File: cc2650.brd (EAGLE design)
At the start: 50.8 x 22.9 mm, 19 parts, among them IC1 TPS73133DBVR, IC4 CC2650MODAMOHR, SW1 SPST_TACT-KMR2, SW3 SPST_TACT-KMR2

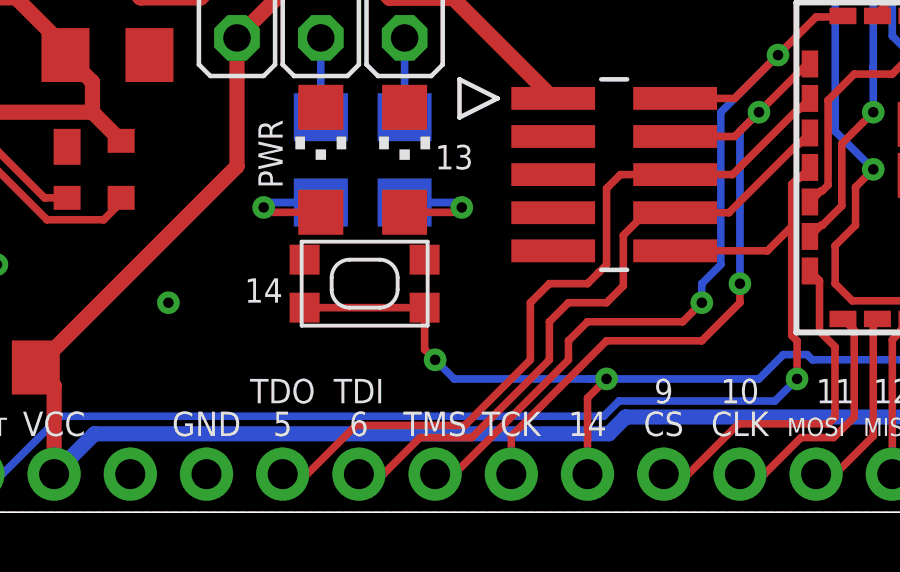
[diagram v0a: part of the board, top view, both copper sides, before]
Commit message: moved gpio button down from LEDs. reduced 'Team Rocket' font size on back so it doesn't interfere with resistors on back.
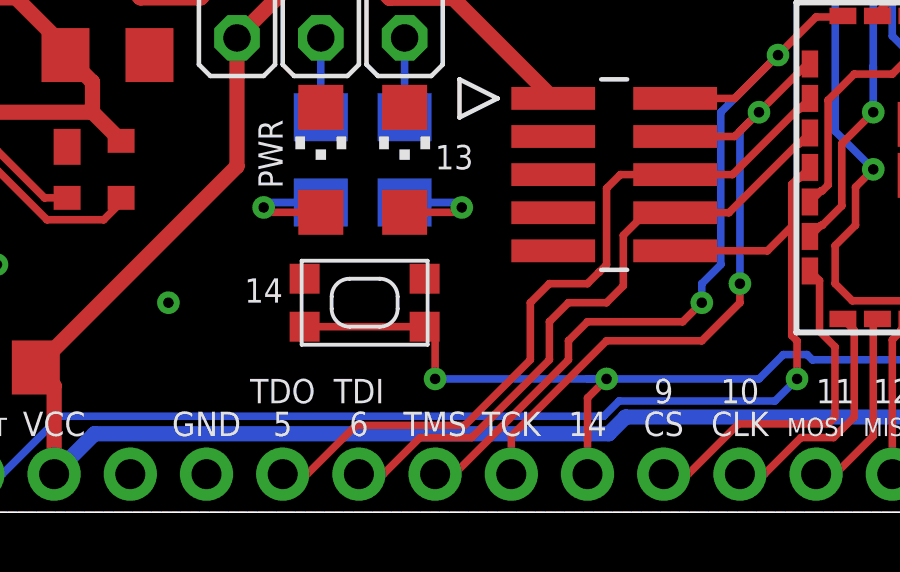
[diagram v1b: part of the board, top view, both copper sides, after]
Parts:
- moved SW3 0.63 mm to (19.2, 6.99)

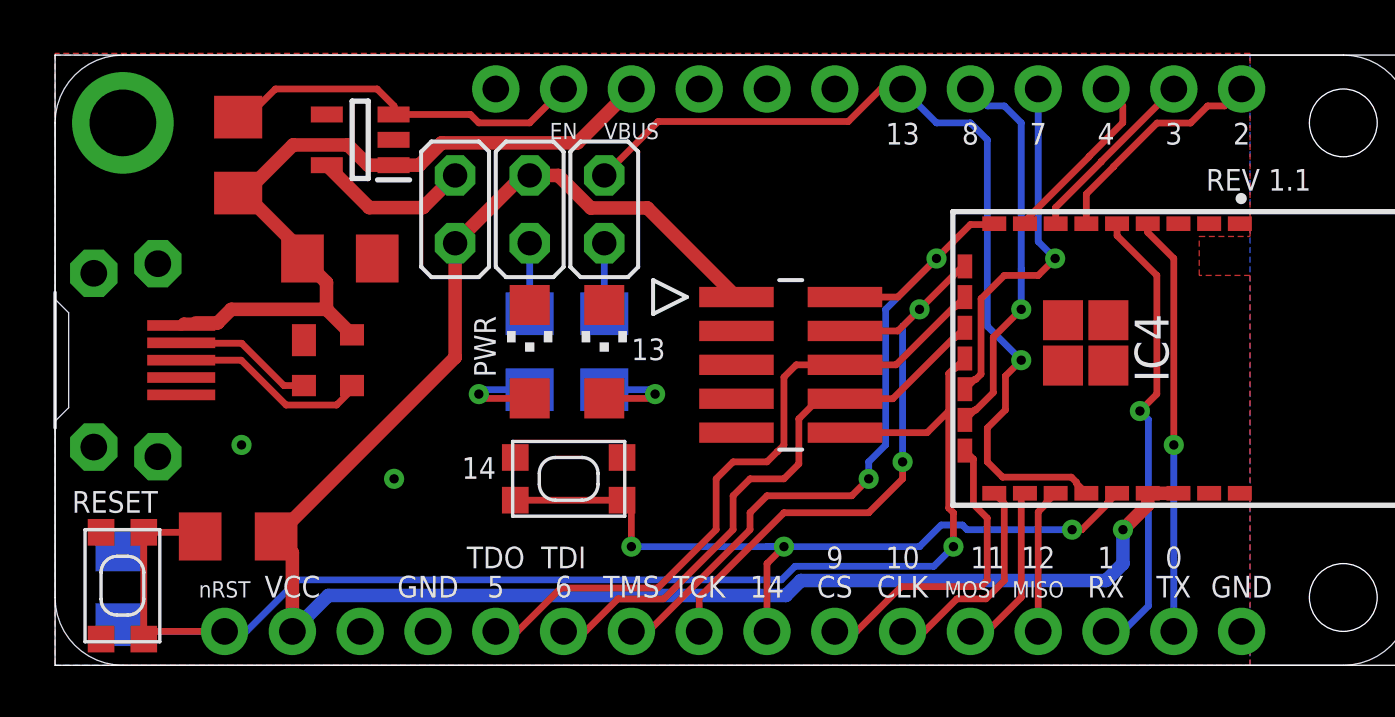
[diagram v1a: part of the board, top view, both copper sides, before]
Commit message: added extra gnd plane vias
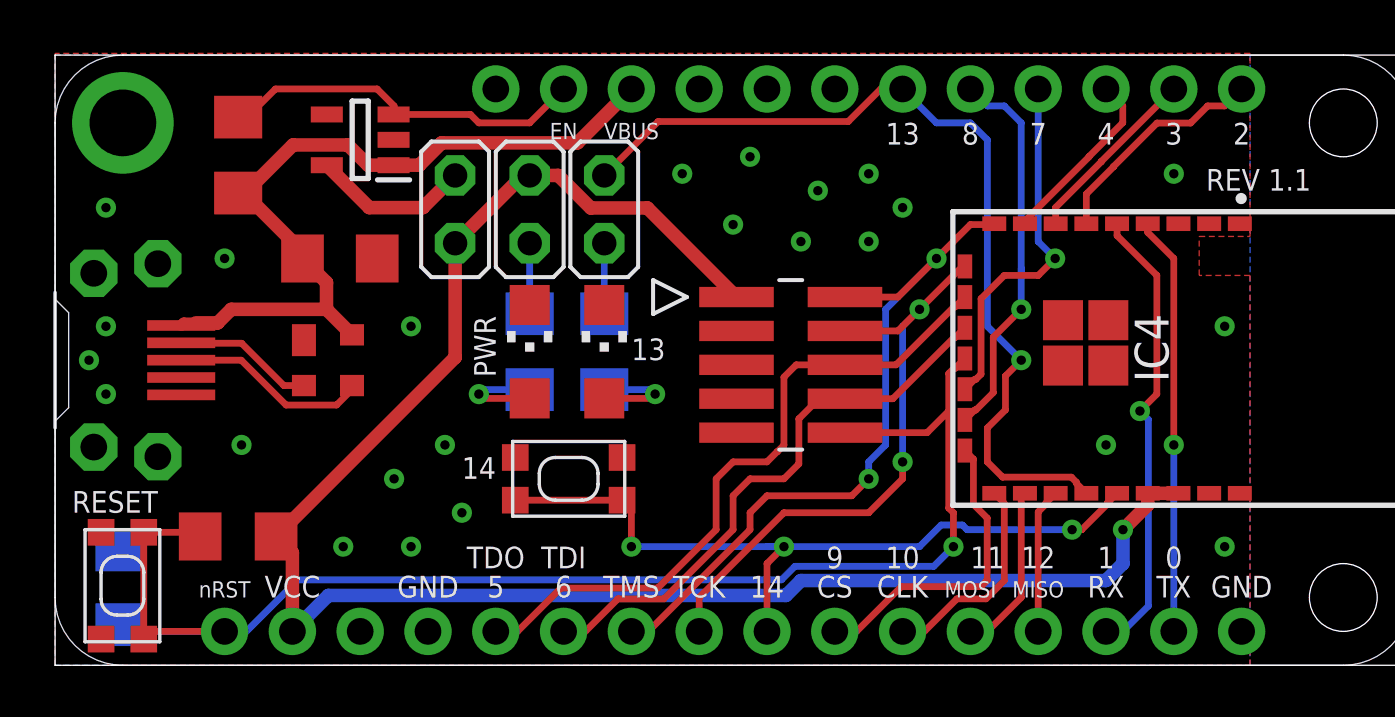
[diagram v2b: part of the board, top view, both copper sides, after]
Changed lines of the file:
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@@
 <via x="6.985" y="8.255" extent="1-16" drill="0.35"/>
 <via x="12.7" y="6.985" extent="1-16" drill="0.35"/>
+<via x="1.905" y="17.145" extent="1-16" drill="0.35"/>
+<via x="6.35" y="15.24" extent="1-16" drill="0.35"/>
+<via x="1.905" y="12.7" extent="1-16" drill="0.35"/>
+<via x="1.27" y="11.43" extent="1-16" drill="0.35"/>
+<via x="1.905" y="10.16" extent="1-16" drill="0.35"/>
+<via x="10.795" y="4.445" extent="1-16" drill="0.35"/>
+<via x="13.335" y="4.445" extent="1-16" drill="0.35"/>
+<via x="15.24" y="5.715" extent="1-16" drill="0.35"/>
+<via x="14.605" y="8.255" extent="1-16" drill="0.35"/>
+<via x="13.335" y="12.7" extent="1-16" drill="0.35"/>
+<via x="23.495" y="18.415" extent="1-16" drill="0.35"/>
+<via x="26.035" y="19.05" extent="1-16" drill="0.35"/>
+<via x="25.4" y="16.51" extent="1-16" drill="0.35"/>
+<via x="27.94" y="15.875" extent="1-16" drill="0.35"/>
+<via x="28.575" y="17.78" extent="1-16" drill="0.35"/>
+<via x="30.48" y="18.415" extent="1-16" drill="0.35"/>
+<via x="31.75" y="17.145" extent="1-16" drill="0.35"/>
+<via x="30.48" y="15.875" extent="1-16" drill="0.35"/>
+<via x="41.91" y="18.415" extent="1-16" drill="0.35"/>
+<via x="43.815" y="12.7" extent="1-16" drill="0.35"/>
+<via x="39.37" y="8.255" extent="1-16" drill="0.35"/>
+<via x="43.815" y="4.445" extent="1-16" drill="0.35"/>
+<wire x1="44.384" y1="6.4435" x2="43.815" y2="4.445" width="0" layer="19" extent="1-1"/>
 </signal>
 <signal name="NRESET">

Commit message: added light sensor to schematic, but not placed on board. Cleaned up text on schematic.
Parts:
- added C1: 100n, adafruit:C0805
- added R4, R6: 10k, adafruit:R0603
- added U1: Value, OPT3001:DNP0006A
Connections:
- net DIO2: now also R4.1, U1.4
- net DIO3: now also R6.1, U1.6
- net GND: now also C1.2, U1.3, U1.7
- net VCC: now also C1.1, R4.2, R6.2, U1.1, U1.2
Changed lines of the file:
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@@
 </element>
 <element name="U$2" library="AMP_Ruler-LT1370" package="2040002" value="2040002" x="0" y="11.43" smashed="yes" rot="R270"/>
+<element name="U1" library="OPT3001" package="DNP0006A" value="Value" x="-14.605" y="-11.43">
+<attribute name="APPLICATION_BUILDNUMBER" value="*" x="-14.605" y="-11.43" size="1.778" layer="27" display="off"/>
+<attribute name="COMPTYPE" value="IC" x="-14.605" y="-11.43" size="1.778" layer="27" display="off"/>
+<attribute name="MANUFACTURER" value="Texas Instruments" x="-14.605" y="-11.43" size="1.778" layer="27" display="off"/>
+<attribute name="MOUNTTYPE" value="SMT" x="-14.605" y="-11.43" size="1.778" layer="27" display="off"/>
+<attribute name="PACKAGEREFERENCE" value="DNP0006A" x="-14.605" y="-11.43" size="1.778" layer="27" display="off"/>
+<attribute name="PARTNUMBER" value="OPT3001DNP" x="-14.605" y="-11.43" size="1.778" layer="27" display="off"/>
+<attribute name="PIN_COUNT" value="7" x="-14.605" y="-11.43" size="1.778" layer="27" display="off"/>
+<attribute name="REFDES" value="RefDes" x="-14.605" y="-11.43" size="1.778" layer="27" display="off"/>
+<attribute name="ROHS" value="Y" x="-14.605" y="-11.43" size="1.778" layer="27" display="off"/>
+<attribute name="TYPE" value="TYPE" x="-14.605" y="-11.43" size="1.778" layer="27" display="off"/>
+</element>
+<element name="R4" library="adafruit" package="R0603" value="10k" x="-8.89" y="-16.51">
+<attribute name="MF" value="" x="-14.605" y="-16.51" size="1.778" layer="27" display="off"/>
+<attribute name="MPN" value="RC0603JR-07100KL" x="-14.605" y="-16.51" size="1.778" layer="27" display="off"/>
+<attribute name="OC_NEWARK" value="68R0147" x="-14.605" y="-16.51" size="1.778" layer="27" display="off"/>
+</element>
+<element name="R6" library="adafruit" package="R0603" value="10k" x="-14.605" y="-22.86">
+<attribute name="MF" value="" x="-14.605" y="-22.225" size="1.778" layer="27" display="off"/>
+<attribute name="MPN" value="RC0603JR-07100KL" x="-14.605" y="-22.225" size="1.778" layer="27" display="off"/>
+<attribute name="OC_NEWARK" value="68R0147" x="-14.605" y="-22.225" size="1.778" layer="27" display="off"/>
+</element>
+<element name="C1" library="adafruit" package="C0805" value="100n" x="-13.97" y="-17.145">
+<attribute name="MF" value="" x="-13.97" y="-27.94" size="1.778" layer="27" display="off"/>
+<attribute name="MPN" value="C0805C105K5RACTU" x="-13.97" y="-27.94" size="1.778" layer="27" display="off"/>
+<attribute name="OC_NEWARK" value="05AC8016" x="-13.97" y="-27.94" size="1.778" layer="27" display="off"/>
+</element>
 </elements>
 <signals>
@@
 <via x="39.37" y="8.255" extent="1-16" drill="0.35"/>
 <via x="43.815" y="4.445" extent="1-16" drill="0.35"/>
+<contactref element="U1" pad="3"/>
+<contactref element="U1" pad="7"/>
+<contactref element="C1" pad="2"/>
+<wire x1="42.084" y1="16.5435" x2="44.384" y2="16.5435" width="0" layer="19" extent="1-1"/>
+<wire x1="41.91" y1="18.415" x2="42.084" y2="16.5435" width="0" layer="19" extent="1-1"/>
+<wire x1="43.815" y1="12.7" x2="44.384" y2="16.5435" width="0" layer="19" extent="1-1"/>
+<wire x1="39.459" y1="12.9285" x2="43.815" y2="12.7" width="0" layer="19" extent="1-1"/>
+<wire x1="37.759" y1="12.9285" x2="39.459" y2="12.9285" width="0" layer="19" extent="1-1"/>
+<wire x1="39.459" y1="11.2285" x2="39.459" y2="12.9285" width="0" layer="19" extent="1-1"/>
+<wire x1="37.759" y1="11.2285" x2="37.759" y2="12.9285" width="0" layer="19" extent="1-1"/>
+<wire x1="39.37" y1="8.255" x2="39.459" y2="11.2285" width="0" layer="19" extent="1-1"/>
+<wire x1="44.384" y1="6.4435" x2="39.37" y2="8.255" width="0" layer="19" extent="1-1"/>
+<wire x1="43.815" y1="4.445" x2="44.384" y2="6.4435" width="0" layer="19" extent="1-1"/>
+<wire x1="44.45" y1="1.27" x2="43.815" y2="4.445" width="0" layer="19" extent="1-1"/>
+<wire x1="31.75" y1="17.145" x2="37.759" y2="12.9285" width="0" layer="19" extent="1-1"/>
+<wire x1="30.48" y1="18.415" x2="31.75" y2="17.145" width="0" layer="19" extent="1-1"/>
+<wire x1="30.48" y1="15.875" x2="31.75" y2="17.145" width="0" layer="19" extent="1-1"/>
+<wire x1="28.575" y1="17.78" x2="30.48" y2="18.415" width="0" layer="19" extent="1-1"/>
+<wire x1="27.94" y1="15.875" x2="28.575" y2="17.78" width="0" layer="19" extent="1-1"/>
+<wire x1="25.4" y1="16.51" x2="27.94" y2="15.875" width="0" layer="19" extent="1-1"/>
+<wire x1="26.035" y1="19.05" x2="25.4" y2="16.51" width="0" layer="19" extent="1-1"/>
+<wire x1="23.495" y1="18.415" x2="26.035" y2="19.05" width="0" layer="19" extent="1-1"/>
+<wire x1="25.527" y1="12.525" x2="25.4" y2="16.51" width="0" layer="19" extent="1-1"/>
+<wire x1="25.527" y1="11.255" x2="25.527" y2="12.525" width="0" layer="19" extent="1-1"/>
+<wire x1="25.527" y1="8.715" x2="25.527" y2="11.255" width="0" layer="19" extent="1-1"/>
+<wire x1="21.2405" y1="7.785" x2="25.527" y2="8.715" width="0" layer="19" extent="1-1"/>
+<wire x1="17.2405" y1="7.785" x2="21.2405" y2="7.785" width="0" layer="19" extent="1-1"/>
+<wire x1="14.605" y1="8.255" x2="17.2405" y2="7.785" width="0" layer="19" extent="1-1"/>
+<wire x1="12.7" y1="6.985" x2="14.605" y2="8.255" width="0" layer="19" extent="1-1"/>
+<wire x1="15.24" y1="5.715" x2="14.605" y2="8.255" width="0" layer="19" extent="1-1"/>
+<wire x1="13.335" y1="4.445" x2="15.24" y2="5.715" width="0" layer="19" extent="1-1"/>
+<wire x1="10.795" y1="4.445" x2="13.335" y2="4.445" width="0" layer="19" extent="1-1"/>
+<wire x1="13.97" y1="1.27" x2="13.335" y2="4.445" width="0" layer="19" extent="1-1"/>
+<wire x1="13.335" y1="12.7" x2="14.605" y2="8.255" width="0" layer="19" extent="1-1"/>
+<wire x1="12.068" y1="15.24" x2="13.335" y2="12.7" width="0" layer="19" extent="1-1"/>
+<wire x1="9.3235" y1="12.18" x2="13.335" y2="12.7" width="0" layer="19" extent="1-1"/>
+<wire x1="6.35" y1="15.24" x2="9.3235" y2="12.18" width="0" layer="19" extent="1-1"/>
+<wire x1="12.68" y1="19.685" x2="12.068" y2="15.24" width="0" layer="19" extent="1-1"/>
+<wire x1="10.18" y1="20.635" x2="12.68" y2="19.685" width="0" layer="19" extent="1-1"/>
+<wire x1="17.78" y1="13.4975" x2="13.335" y2="12.7" width="0" layer="19" extent="1-1"/>
+<wire x1="20.574" y1="13.4975" x2="17.78" y2="13.4975" width="0" layer="19" extent="1-1"/>
+<wire x1="6.985" y1="8.255" x2="9.3235" y2="12.18" width="0" layer="19" extent="1-1"/>
+<wire x1="4.725" y1="10.13" x2="6.985" y2="8.255" width="0" layer="19" extent="1-1"/>
+<wire x1="1.905" y1="10.16" x2="4.725" y2="10.13" width="0" layer="19" extent="1-1"/>
+<wire x1="1.27" y1="11.43" x2="1.905" y2="10.16" width="0" layer="19" extent="1-1"/>
+<wire x1="1.905" y1="12.7" x2="1.27" y2="11.43" width="0" layer="19" extent="1-1"/>
+<wire x1="1.905" y1="17.145" x2="1.905" y2="12.7" width="0" layer="19" extent="1-1"/>
+<wire x1="1.723" y1="4.9815" x2="1.905" y2="10.16" width="0" layer="19" extent="1-1"/>
+<wire x1="2.413" y1="4.321" x2="1.723" y2="4.9815" width="0" layer="19" extent="1-16"/>
+<wire x1="1.723" y1="0.9815" x2="2.413" y2="4.321" width="0" layer="19" extent="1-16"/>
+<wire x1="-14.605" y1="-11.43" x2="1.723" y2="0.9815" width="0" layer="19" extent="1-1"/>
+<wire x1="-15.555" y1="-12.085" x2="-14.605" y2="-11.43" width="0" layer="19" extent="1-1"/>
+<wire x1="-13.12" y1="-17.145" x2="-15.555" y2="-12.085" width="0" layer="19" extent="1-1"/>
 </signal>
 <signal name="NRESET">
@@
 <wire x1="43.815" y1="20.955" x2="44.45" y2="21.59" width="0.254" layer="1"/>
 <wire x1="38.634" y1="17.6558375" x2="39.6494" y2="18.6712375" width="0.254" layer="1"/>
+<contactref element="U1" pad="4"/>
+<contactref element="R4" pad="1"/>
+<wire x1="-9.74" y1="-16.51" x2="38.634" y2="16.5435" width="0" layer="19" extent="1-1"/>
+<wire x1="-13.655" y1="-12.08" x2="-9.74" y2="-16.51" width="0" layer="19" extent="1-1"/>
 </signal>
 <signal name="DIO3">
@@
 <wire x1="39.1922" y1="18.86061875" x2="39.1922" y2="18.8722" width="0.254" layer="1"/>
 <wire x1="39.1922" y1="18.8722" x2="41.91" y2="21.59" width="0.254" layer="1"/>
+<contactref element="R6" pad="1"/>
+<contactref element="U1" pad="6"/>
+<wire x1="-13.655" y1="-10.78" x2="37.484" y2="16.5435" width="0" layer="19" extent="1-1"/>
+<wire x1="-15.455" y1="-22.86" x2="-13.655" y2="-10.78" width="0" layer="19" extent="1-1"/>
 </signal>
 <signal name="DIO4">
@@
 <wire x1="20.0689875" y1="17.1323" x2="22.1897" y2="17.1323" width="0.508" layer="1"/>
 <wire x1="22.1897" y1="17.1323" x2="25.527" y2="13.795" width="0.508" layer="1"/>
+<contactref element="R4" pad="2"/>
+<contactref element="R6" pad="2"/>
+<contactref element="U1" pad="2"/>
+<contactref element="U1" pad="1"/>
+<contactref element="C1" pad="1"/>
+<wire x1="-14.82" y1="-17.145" x2="-13.755" y2="-22.86" width="0" layer="19" extent="1-1"/>
+<wire x1="-15.555" y1="-11.43" x2="-14.82" y2="-17.145" width="0" layer="19" extent="1-1"/>
+<wire x1="-15.555" y1="-10.78" x2="-15.555" y2="-11.43" width="0" layer="19" extent="1-1"/>
+<wire x1="-8.04" y1="-16.51" x2="-14.82" y2="-17.145" width="0" layer="19" extent="1-1"/>
+<wire x1="8.89" y1="1.27" x2="-8.04" y2="-16.51" width="0" layer="19" extent="1-16"/>
 </signal>
 <signal name="VBUS" class="2">

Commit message: moved light sensor to board and added VCC connections.
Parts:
- added R7: 715, adafruit:R1206
- moved R6 57.5 mm to (27.3, 16.5), turned to 180 degrees
- moved U1 54.0 mm to (30.6, 18.1)
- moved C1 52.8 mm to (24.7, 18.9)
- moved R4 49.0 mm to (27.3, 16.5), flipped to the bottom
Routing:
- net VCC: track 67.4 -> 88.6 mm
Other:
- board text added: "REV 2.0"
- board text removed: "REV 1.1"

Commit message: Removed text from light sensor and changed sensor position.
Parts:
- moved U1 21.5 mm to (12.8, 6.03)
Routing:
- net VCC: track 88.6 -> 92.6 mm
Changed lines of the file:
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@@
 </element>
 <element name="U$2" library="AMP_Ruler-LT1370" package="2040002" value="2040002" x="0" y="11.43" smashed="yes" rot="R270"/>
-<element name="U1" library="OPT3001" package="DNP0006A" value="Value" x="30.607" y="18.0975" smashed="yes">
-<attribute name="APPLICATION_BUILDNUMBER" value="*" x="30.607" y="18.0975" size="1.778" layer="27" display="off"/>
-<attribute name="COMPTYPE" value="IC" x="30.607" y="18.0975" size="1.778" layer="27" display="off"/>
-<attribute name="MANUFACTURER" value="Texas Instruments" x="30.607" y="18.0975" size="1.778" layer="27" display="off"/>
-<attribute name="MOUNTTYPE" value="SMT" x="30.607" y="18.0975" size="1.778" layer="27" display="off"/>
-<attribute name="PACKAGEREFERENCE" value="DNP0006A" x="30.607" y="18.0975" size="1.778" layer="27" display="off"/>
-<attribute name="PARTNUMBER" value="OPT3001DNP" x="30.607" y="18.0975" size="1.778" layer="27" display="off"/>
-<attribute name="PIN_COUNT" value="7" x="30.607" y="18.0975" size="1.778" layer="27" display="off"/>
-<attribute name="REFDES" value="RefDes" x="30.607" y="18.0975" size="1.778" layer="27" display="off"/>
-<attribute name="ROHS" value="Y" x="30.607" y="18.0975" size="1.778" layer="27" display="off"/>
-<attribute name="TYPE" value="TYPE" x="30.607" y="18.0975" size="1.778" layer="27" display="off"/>
+<element name="U1" library="OPT3001" package="DNP0006A" value="Value" x="12.827" y="6.0325" smashed="yes">
+<attribute name="APPLICATION_BUILDNUMBER" value="*" x="12.827" y="6.0325" size="1.778" layer="27" display="off"/>
+<attribute name="COMPTYPE" value="IC" x="12.827" y="6.0325" size="1.778" layer="27" display="off"/>
+<attribute name="MANUFACTURER" value="Texas Instruments" x="12.827" y="6.0325" size="1.778" layer="27" display="off"/>
+<attribute name="MOUNTTYPE" value="SMT" x="12.827" y="6.0325" size="1.778" layer="27" display="off"/>
+<attribute name="PACKAGEREFERENCE" value="DNP0006A" x="12.827" y="6.0325" size="1.778" layer="27" display="off"/>
+<attribute name="PARTNUMBER" value="OPT3001DNP" x="12.827" y="6.0325" size="1.778" layer="27" display="off"/>
+<attribute name="PIN_COUNT" value="7" x="12.827" y="6.0325" size="1.778" layer="27" display="off"/>
+<attribute name="REFDES" value="RefDes" x="12.827" y="6.0325" size="1.778" layer="27" display="off"/>
+<attribute name="ROHS" value="Y" x="12.827" y="6.0325" size="1.778" layer="27" display="off"/>
+<attribute name="TYPE" value="TYPE" x="12.827" y="6.0325" size="1.778" layer="27" display="off"/>
 </element>
 <element name="R4" library="adafruit" package="R0603" value="10k" x="27.305" y="16.51" smashed="yes" rot="MR0">
@@
 <contactref element="U1" pad="4"/>
 <contactref element="R4" pad="1"/>
-<wire x1="31.557" y1="17.4475" x2="38.634" y2="17.6558375" width="0" layer="19" extent="1-1"/>
-<wire x1="28.155" y1="16.51" x2="31.557" y2="17.4475" width="0" layer="19" extent="1-16"/>
+<wire x1="28.155" y1="16.51" x2="38.634" y2="16.5435" width="0" layer="19" extent="1-16"/>
+<wire x1="13.777" y1="5.3825" x2="28.155" y2="16.51" width="0" layer="19" extent="1-16"/>
 </signal>
 <signal name="DIO3">
@@
 <contactref element="R6" pad="1"/>
 <contactref element="U1" pad="6"/>
-<wire x1="31.557" y1="18.7475" x2="37.484" y2="17.15241875" width="0" layer="19" extent="1-1"/>
-<wire x1="28.155" y1="16.51" x2="31.557" y2="18.7475" width="0" layer="19" extent="1-1"/>
+<wire x1="28.155" y1="16.51" x2="37.484" y2="16.5435" width="0" layer="19" extent="1-1"/>
+<wire x1="13.777" y1="6.6825" x2="28.155" y2="16.51" width="0" layer="19" extent="1-1"/>
 </signal>
 <signal name="DIO4">
@@
 <wire x1="18.8497875" y1="18.3515" x2="20.0689875" y2="17.1323" width="0.508" layer="1"/>
 <wire x1="8.89" y1="1.27" x2="8.89" y2="4.216" width="0.508" layer="1"/>
-<wire x1="8.28" y1="4.826" x2="8.89" y2="4.216" width="0.508" layer="1"/>
+<wire x1="8.89" y1="4.216" x2="8.28" y2="4.826" width="0.508" layer="1"/>
 <wire x1="17.78" y1="18.3515" x2="17.526" y2="18.3515" width="0.508" layer="1"/>
 <wire x1="17.526" y1="18.3515" x2="14.986" y2="15.8115" width="0.508" layer="1"/>
@@
 <wire x1="22.1897" y1="17.1323" x2="25.8327" y2="17.1323" width="0.508" layer="1"/>
 <wire x1="25.8327" y1="17.1323" x2="26.455" y2="16.51" width="0.508" layer="1"/>
-<wire x1="29.5842" y1="18.0247" x2="29.657" y2="18.0975" width="0.508" layer="1"/>
 <wire x1="25.8327" y1="17.1323" x2="27.08071875" y2="17.1323" width="0.508" layer="1"/>
 <wire x1="27.08071875" y1="17.1323" x2="27.97311875" y2="18.0247" width="0.508" layer="1"/>
 <wire x1="27.97311875" y1="18.0247" x2="29.5842" y2="18.0247" width="0.508" layer="1"/>
-<wire x1="29.657" y1="18.0975" x2="29.657" y2="18.7475" width="0.508" layer="1"/>
+<wire x1="11.877" y1="6.0325" x2="11.877" y2="6.6825" width="0.508" layer="1"/>
+<wire x1="8.28" y1="4.826" x2="10.6705" y2="4.826" width="0.508" layer="1"/>
+<wire x1="10.6705" y1="4.826" x2="11.877" y2="6.0325" width="0.508" layer="1"/>
 </signal>
 <signal name="VBUS" class="2">
